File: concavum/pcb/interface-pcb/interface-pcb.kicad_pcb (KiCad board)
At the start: 2 copper layers, 29 x 40 mm, 19 parts, among them J1 PJ-342CB-TX-SMT, P1 ISP Pads, U1 ATMEGA32U4-MUR, U3 MCP23017-E/SO, X1 16MHz

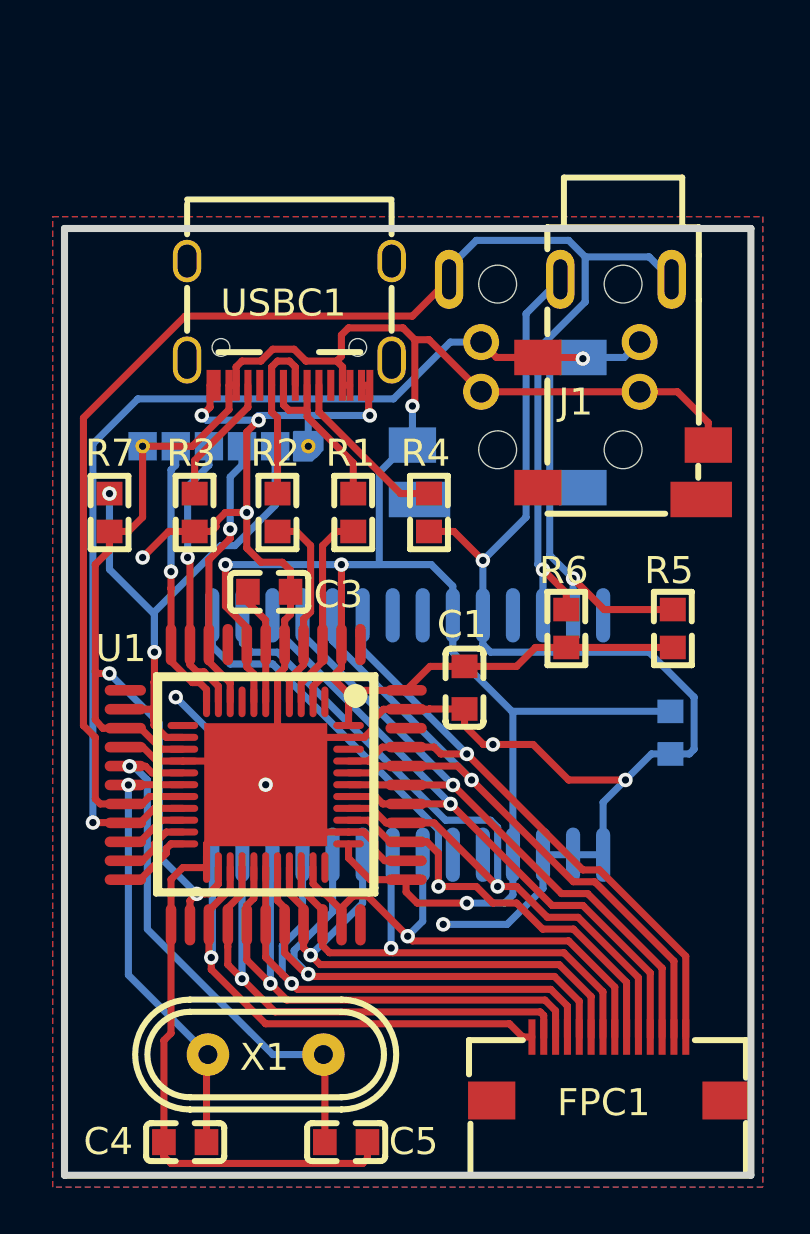
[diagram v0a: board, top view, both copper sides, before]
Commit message: Redo interface PCB using KiCad
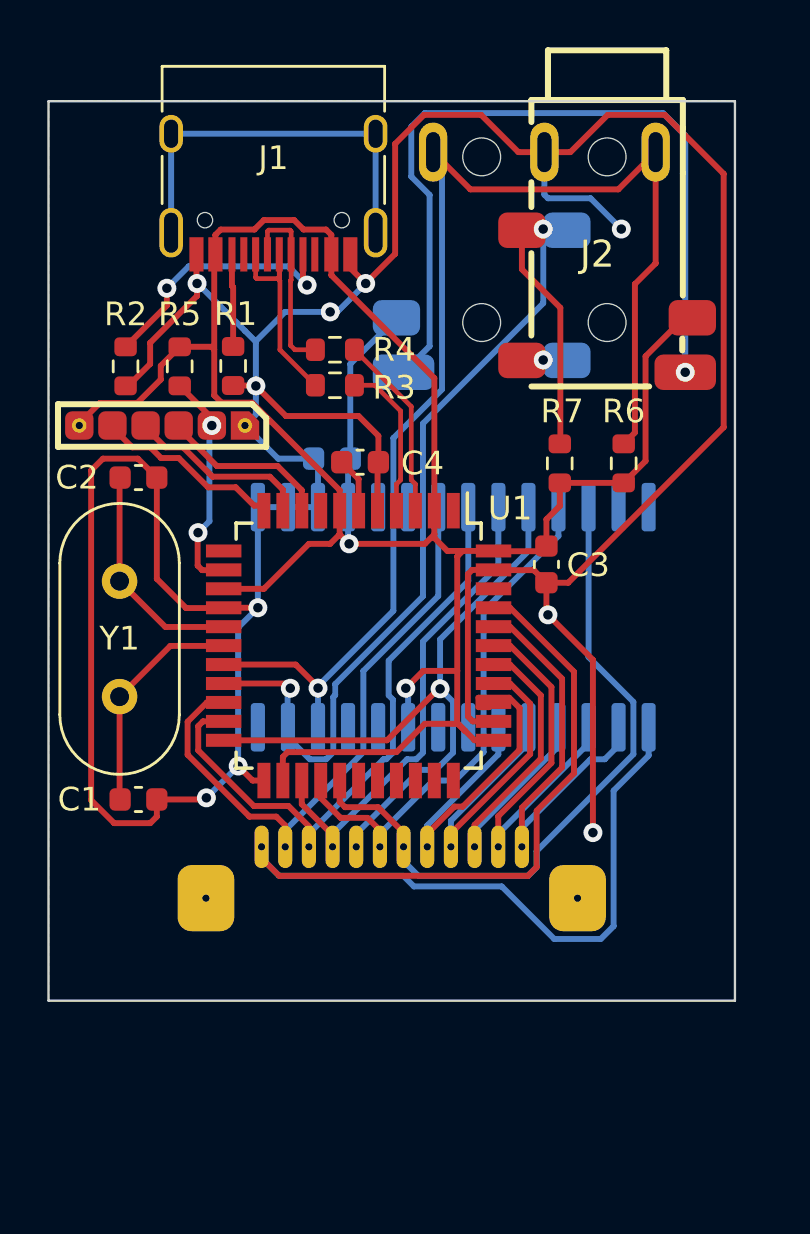
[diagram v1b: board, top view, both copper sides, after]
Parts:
- removed FPC1: AFC01-S14FCC-00, easyeda:FPC-SMD_14P-P0.50_AFC01-S14FCC-00
- removed P1: ISP Pads, easyeda:ISP PADS
- removed U3: MCP23017-E/SO, easyeda:SOIC-28_L18.1-W10.3-P1.27-LS10.3-BL
- removed USBC1: TYPE-C-31-M-12, easyeda:USB-C_SMD-TYPE-C-31-M-12
- removed X1: 16MHz, easyeda:HC-49US_L11.0-W4.6-P4.88
- added J2: Audio_Jack, Custom:Audio-Jack-Dual-Side, F.Cu at (163.6, 86.8)
- added J3: ISP_pads, Custom:ISP-Pads, F.Cu at (148.3, 93.7)
- added J4: FPC_connector, Custom:FPC-Connector, F.Cu at (154.5, 111.5)
- added U2: MCP23017_SO, Package_SO:SOIC-28W_7.5x17.9mm_P1.27mm, B.Cu at (157.1, 101.8)
- added Y1: Crystal_16MHz, Crystal:Crystal_HC49-4H_Vertical, F.Cu at (143.0, 105.2)
- C1, C2: value 100n -> 22p; footprint easyeda:C0603 -> Capacitor_SMD:C_0603_1608Metric
- C3: value 1u -> 100n; footprint easyeda:C0603 -> Capacitor_SMD:C_0603_1608Metric
- C4: value 22p -> 1u; footprint easyeda:C0603 -> Capacitor_SMD:C_0603_1608Metric
- C5: value 22p -> 100n; footprint easyeda:C0603 -> Capacitor_SMD:C_0603_1608Metric; moved to B.Cu
- J1: value PJ-342CB-TX-SMT -> USB_C_Port; footprint easyeda:AUDIO-SMD_PJ-342CB-TX-SMT DUAL SIDE HOLES -> Connector_USB:USB_C_Receptacle_HRO_TYPE-C-31-M-12
- R1, R2: value 22 -> 5.1k; footprint easyeda:R0603 -> Resistor_SMD:R_0603_1608Metric
- R3, R4: value 5.1k -> 22; footprint easyeda:R0603 -> Resistor_SMD:R_0603_1608Metric
- R5: value 1k -> 5.1k; footprint easyeda:R0603 -> Resistor_SMD:R_0603_1608Metric
- R6: footprint easyeda:R0603 -> Resistor_SMD:R_0603_1608Metric
- R7: value 5.1k -> 1k; footprint easyeda:R0603 -> Resistor_SMD:R_0603_1608Metric
- U1: value ATMEGA32U4-MUR -> ATmega32U4-A; footprint easyeda:QFN-44 QFP-44 -> Package_QFP:TQFP-44_10x10mm_P0.8mm
- moved C4 29.7 mm to (153.2, 95.2)
- moved C5 28.9 mm to (152.0, 95.1)
- moved C2 24.9 mm to (143.8, 95.9), turned to 0 degrees
- moved R5 23.6 mm to (145.5, 91.2), turned to 90 degrees
- moved R7 19.1 mm to (161.6, 95.3)
- moved J1 17.7 mm to (149.5, 82.4), turned to 180 degrees
- moved C1 14.6 mm to (143.8, 109.5), turned to 0 degrees
- moved C3 11.8 mm to (161.0, 99.6), turned to -90 degrees
- moved R2 8.91 mm to (143.3, 91.2), turned to -90 degrees
- moved R1 8.00 mm to (147.8, 91.2), turned to -90 degrees
- moved R3 8.00 mm to (152.1, 92.0), turned to 0 degrees
- moved R4 7.94 mm to (152.1, 90.5), turned to 0 degrees
- moved R6 7.39 mm to (164.3, 95.3)
- moved U1 7.07 mm to (153.1, 103.0), turned to -90 degrees
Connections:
- C1 pad 1: GND -> /XTAL1
- C1 pad 2: +5V -> GND
- C2 pad 1: GND -> /XTAL2
- C2 pad 2: +5V -> GND
- C3 pad 1: GND -> +5V
- C3 pad 2: U1_6 -> GND
- C4 pad 1: GND -> Net-(C4-Pad1)
- C4 pad 2: XTAL1 -> GND
- C5 pad 1: GND -> +5V
- C5 pad 2: XTAL2 -> GND
- R1 pad 1: RD- -> Net-(J1-PadB5)
- R1 pad 2: D- -> GND
- R2 pad 1: RD+ -> Net-(J1-PadA5)
- R2 pad 2: D+ -> GND
- R3 pad 1: GND -> /D+
- R3 pad 2: USBC1_B5 -> /DR+
- R4 pad 1: GND -> /D-
- R4 pad 2: USBC1_A5 -> /DR-
- R5 pad 1: SDA -> /RST
- R6 pad 1: SCL -> /SCL
- R7 pad 1: RST -> /SDA
- U1 pad 1: (no net) -> unconnected-(U1-Pad1)
- U1 pad 10: MOSI -> /MOSI
- U1 pad 11: MISO -> /MISO
- U1 pad 12: (no net) -> unconnected-(U1-Pad12)
- U1 pad 13: RST -> /RST
- U1 pad 16: XTAL2 -> /XTAL2
- U1 pad 17: XTAL1 -> /XTAL1
- U1 pad 18: SCL -> /SCL
- U1 pad 19: SDA -> /SDA
- U1 pad 20: (no net) -> /COL1
- U1 pad 21: (no net) -> /COL2
- U1 pad 22: (no net) -> /COL4
- U1 pad 25: COL1 -> /COL3
- U1 pad 26: COL2 -> /COL5
- U1 pad 27: COL3 -> /COL6
- U1 pad 28: COL4 -> unconnected-(U1-Pad28)
- U1 pad 29: COL5 -> unconnected-(U1-Pad29)
- U1 pad 3: RD- -> /DR-
- U1 pad 30: COL6 -> unconnected-(U1-Pad30)
- U1 pad 31: COL7 -> unconnected-(U1-Pad31)
- U1 pad 32: COL8 -> unconnected-(U1-Pad32)
- U1 pad 33: (no net) -> unconnected-(U1-Pad33)
- U1 pad 36: ROW1 -> /ROW2
- U1 pad 37: ROW2 -> /ROW3
- U1 pad 38: ROW3 -> /ROW4
- U1 pad 39: ROW4 -> /ROW5
- U1 pad 4: RD+ -> /DR+
- U1 pad 40: ROW5 -> /ROW6
- U1 pad 41: ROW6 -> /ROW1
- U1 pad 42: (no net) -> unconnected-(U1-Pad42)
- U1 pad 6: U1_6 -> Net-(C4-Pad1)
- U1 pad 8: (no net) -> unconnected-(U1-Pad8)
- U1 pad 9: SCK -> /SCK
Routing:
- net SCL: track 67.3 -> 0.00 mm, vias 1 -> 0
- net SDA: track 62.8 -> 0.00 mm, vias 3 -> 0
- net /SCL: track 0.00 -> 54.6 mm, vias 0 -> 1
- net /ROW1: track 0.00 -> 52.0 mm
- net /SDA: track 0.00 -> 42.9 mm, vias 0 -> 2
- net +5V: track 145.6 -> 104.9 mm, vias 6 -> 2
- net ROW2: track 35.4 -> 0.00 mm, vias 1 -> 0
- net ROW1: track 34.2 -> 0.00 mm, vias 1 -> 0
- net unconnected-(J2-PadTN): track 0.00 -> 33.4 mm, vias 0 -> 1
- net ROW5: track 29.9 -> 0.00 mm, vias 1 -> 0
- net ROW3: track 29.6 -> 0.00 mm, vias 1 -> 0
- net ROW6: track 29.2 -> 0.00 mm, vias 1 -> 0
- net ROW4: track 29.2 -> 0.00 mm, vias 1 -> 0
- net /COL6: track 0.00 -> 28.8 mm
- net /COL4: track 0.00 -> 28.2 mm, vias 0 -> 1
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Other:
- board size 29 x 40 mm -> 29 x 38 mm

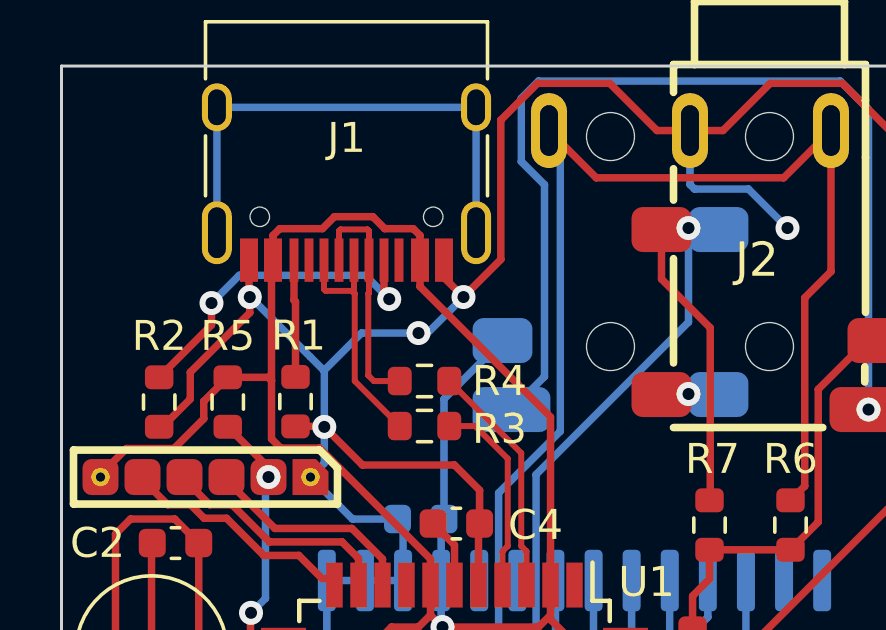
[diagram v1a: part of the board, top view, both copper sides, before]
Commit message: Add a 10µF capacitor as desrcibed in the datasheet
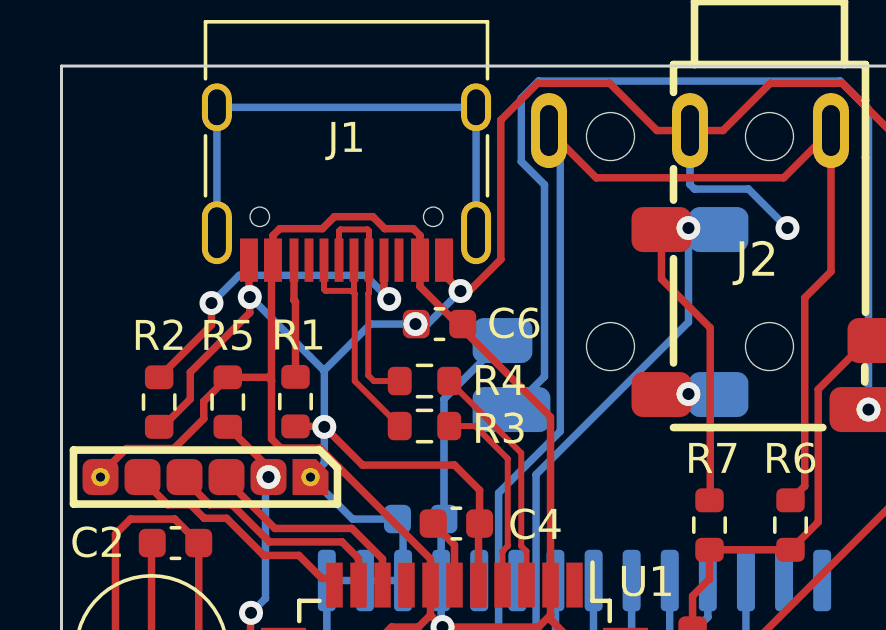
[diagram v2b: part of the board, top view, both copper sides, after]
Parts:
- added C6: 10u, Capacitor_SMD:C_0603_1608Metric, F.Cu at (152.6, 88.6)
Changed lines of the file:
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@@
   (net 52 "unconnected-(J1-PadB8)")
   (net 53 "unconnected-(J1-PadA8)")
+  (footprint "Capacitor_SMD:C_0603_1608Metric" (layer "F.Cu")
+    (at 152.6 88.6 180)
+    (descr "Capacitor SMD 0603 (1608 Metric), square (rectangular) end terminal, IPC_7351 nominal, (Body size source: IPC-SM-782 page 76, https://www.pcb-3d.com/wordpress/wp-content/uploads/ipc-sm-782a_amendment_1_and_2.pdf), generated with kicad-footprint-generator")
+    (tags "capacitor")
+    (property "Sheetfile" "interface-pcb.kicad_sch")
+    (property "Sheetname" "")
+    (attr smd)
+    (fp_text reference "C6" (at -2.5 0) (layer "F.SilkS")
+      (effects (font (size 1 1) (thickness 0.15)))
+    )
+    (fp_text value "10u" (at 2.8 0) (layer "F.Fab")
+      (effects (font (size 1 1) (thickness 0.15)))
+    )
+    (fp_text user "${REFERENCE}" (at 0 0) (layer "F.Fab")
+      (effects (font (size 0.4 0.4) (thickness 0.06)))
+    )
+    (fp_line (start -0.14058 -0.51) (end 0.14058 -0.51) (layer "F.SilkS") (width 0.12))
+    (fp_line (start -0.14058 0.51) (end 0.14058 0.51) (layer "F.SilkS") (width 0.12))
+    (fp_line (start 1.48 -0.73) (end 1.48 0.73) (layer "F.CrtYd") (width 0.05))
+    (fp_line (start -1.48 -0.73) (end 1.48 -0.73) (layer "F.CrtYd") (width 0.05))
+    (fp_line (start -1.48 0.73) (end -1.48 -0.73) (layer "F.CrtYd") (width 0.05))
+    (fp_line (start 1.48 0.73) (end -1.48 0.73) (layer "F.CrtYd") (width 0.05))
+    (fp_line (start -0.8 0.4) (end -0.8 -0.4) (layer "F.Fab") (width 0.1))
+    (fp_line (start 0.8 0.4) (end -0.8 0.4) (layer "F.Fab") (width 0.1))
+    (fp_line (start -0.8 -0.4) (end 0.8 -0.4) (layer "F.Fab") (width 0.1))
+    (fp_line (start 0.8 -0.4) (end 0.8 0.4) (layer "F.Fab") (width 0.1))
+    (pad "1" smd roundrect locked (at -0.775 0 180) (size 0.9 0.95) (layers "F.Cu" "F.Paste" "F.Mask") (roundrect_rratio 0.25)
+      (net 4 "+5V") (pintype "passive"))
+    (pad "2" smd roundrect locked (at 0.775 0 180) (size 0.9 0.95) (layers "F.Cu" "F.Paste" "F.Mask") (roundrect_rratio 0.25)
+      (net 2 "GND") (pintype "passive"))
+    (model "${KICAD6_3DMODEL_DIR}/Capacitor_SMD.3dshapes/C_0603_1608Metric.wrl"
+      (offset (xyz 0 0 0))
+      (scale (xyz 1 1 1))
+      (rotate (xyz 0 0 0))
+    )
+  )
   (footprint "Resistor_SMD:R_0603_1608Metric" (layer "F.Cu")
     (at 143.256 91.2 -90)
@@
   (segment (start 161.036 101.636) (end 161.1 101.7) (width 0.25) (layer "F.Cu") (net 2))
   (segment (start 160.505 99.812) (end 161.036 100.343) (width 0.25) (layer "F.Cu") (net 2))
-  (segment (start 153.4 87.7) (end 153.4 87.691047) (width 0.25) (layer "F.Cu") (net 2))
   (segment (start 144.575 110.225) (end 144.575 109.5) (width 0.25) (layer "F.Cu") (net 2))
   (segment (start 163 103.6) (end 163 110.9) (width 0.25) (layer "F.Cu") (net 2))
   (segment (start 146.25 87.67402) (end 146.27598 87.7) (width 0.25) (layer "F.Cu") (net 2))
   (segment (start 144.29296 91.1) (end 143.36796 92.025) (width 0.25) (layer "F.Cu") (net 2))
-  (segment (start 159.85 82.15) (end 160.95 82.15) (width 0.25) (layer "F.Cu") (net 2))
+  (segment (start 152.75 86.95) (end 152.75 86.47) (width 0.25) (layer "F.Cu") (net 2))
   (segment (start 153.9 95.541) (end 154.191 95.25) (width 0.25) (layer "F.Cu") (net 2))
   (segment (start 146.27598 87.7) (end 146.27598 88.22402) (width 0.25) (layer "F.Cu") (net 2))
   (segment (start 144.575 95.9) (end 143.775 95.1) (width 0.25) (layer "F.Cu") (net 2))
-  (segment (start 154.64452 81.798012) (end 155.867052 80.57548) (width 0.25) (layer "F.Cu") (net 2))
-  (segment (start 153.4 87.7) (end 152.75 87.05) (width 0.25) (layer "F.Cu") (net 2))
-  (segment (start 153.4 87.691047) (end 154.64452 86.446527) (width 0.25) (layer "F.Cu") (net 2))
+  (segment (start 159.85 82.15) (end 160.95 82.15) (width 0.25) (layer "F.Cu") (net 2))
   (segment (start 157.925978 106.2) (end 157.718051 105.992073) (width 0.25) (layer "F.Cu") (net 2))
   (segment (start 146.27598 88.22402) (end 144.29296 90.20704) (width 0.25) (layer "F.Cu") (net 2))
@@
   (segment (start 153.937 95.25) (end 153.937 94.137) (width 0.25) (layer "F.Cu") (net 2))
   (segment (start 148.624598 108.7) (end 148.012299 108.087701) (width 0.25) (layer "F.Cu") (net 2))
-  (segment (start 158.27548 80.57548) (end 159.85 82.15) (width 0.25) (layer "F.Cu") (net 2))
+  (segment (start 153.3 87.5) (end 152.75 86.95) (width 0.25) (layer "F.Cu") (net 2))
+  (segment (start 153.3 87.5) (end 153.591047 87.5) (width 0.25) (layer "F.Cu") (net 2))
+  (segment (start 154.64452 81.798012) (end 155.867052 80.57548) (width 0.25) (layer "F.Cu") (net 2))
+  (segment (start 155.867052 80.57548) (end 158.27548 80.57548) (width 0.25) (layer "F.Cu") (net 2))
   (segment (start 142.3 95.1) (end 141.8 95.6) (width 0.25) (layer "F.Cu") (net 2))
+  (segment (start 153.591047 87.5) (end 154.64452 86.446527) (width 0.25) (layer "F.Cu") (net 2))
   (segment (start 144.575 100.175) (end 144.575 95.9) (width 0.25) (layer "F.Cu") (net 2))
   (segment (start 145.812 101.412) (end 144.575 100.175) (width 0.25) (layer "F.Cu") (net 2))
@@
   (segment (start 148.760218 92.028168) (end 148.74305 92.011) (width 0.25) (layer "F.Cu") (net 2))
   (segment (start 157.718051 105.992073) (end 157.718051 99.981949) (width 0.25) (layer "F.Cu") (net 2))
-  (segment (start 155.867052 80.57548) (end 158.27548 80.57548) (width 0.25) (layer "F.Cu") (net 2))
+  (segment (start 158.27548 80.57548) (end 159.85 82.15) (width 0.25) (layer "F.Cu") (net 2))
+  (segment (start 154.64452 86.446527) (end 154.64452 81.798012) (width 0.25) (layer "F.Cu") (net 2))
   (segment (start 161.1 101.7) (end 163 103.6) (width 0.25) (layer "F.Cu") (net 2))
   (segment (start 153.9 97.082) (end 153.9 95.541) (width 0.25) (layer "F.Cu") (net 2))
   (segment (start 143.36796 92.025) (end 143.256 92.025) (width 0.25) (layer "F.Cu") (net 2))
-  (segment (start 152.75 87.05) (end 152.75 86.47) (width 0.25) (layer "F.Cu") (net 2))
-  (segment (start 154.64452 86.446527) (end 154.64452 81.798012) (width 0.25) (layer "F.Cu") (net 2))
   (segment (start 157.718051 99.981949) (end 157.9 99.8) (width 0.25) (layer "F.Cu") (net 2))
   (segment (start 147.169 101.412) (end 145.812 101.412) (width 0.25) (layer "F.Cu") (net 2))
@@
   (segment (start 161.036 100.343) (end 161.957 100.343) (width 0.25) (layer "F.Cu") (net 2))
   (segment (start 166.032948 80.57548) (end 163.62452 80.57548) (width 0.25) (layer "F.Cu") (net 2))
-  (via (at 151.9 88.9) (size 0.8) (drill 0.4) (layers "F.Cu" "B.Cu") (net 2))
+  (via (at 151.8 88.6) (size 0.8) (drill 0.4) (layers "F.Cu" "B.Cu") (net 2))
   (via (at 161.1 101.7) (size 0.8) (drill 0.4) (layers "F.Cu" "B.Cu") (net 2))
   (via (at 146.27598 87.7) (size 0.8) (drill 0.4) (layers "F.Cu" "B.Cu") (net 2))
@@
   (via (at 163 110.9) (size 0.8) (drill 0.4) (layers "F.Cu" "B.Cu") (net 2))
   (via (at 148.760218 92.028168) (size 0.8) (drill 0.4) (layers "F.Cu" "B.Cu") (net 2))
-  (via (at 153.4 87.7) (size 0.8) (drill 0.4) (layers "F.Cu" "B.Cu") (net 2))
+  (via (at 153.3 87.5) (size 0.8) (drill 0.4) (layers "F.Cu" "B.Cu") (net 2))
   (segment (start 148.845 101.4) (end 148.012299 102.232701) (width 0.25) (layer "B.Cu") (net 2))
+  (segment (start 152.2 88.6) (end 151.8 88.6) (width 0.25) (layer "B.Cu") (net 2))
   (segment (start 151.385 97.15) (end 151.385 95.285) (width 0.25) (layer "B.Cu") (net 2))
   (segment (start 146.669841 109.430159) (end 148.012299 108.087701) (width 0.25) (layer "B.Cu") (net 2))
-  (segment (start 152.2 88.9) (end 151.9 88.9) (width 0.25) (layer "B.Cu") (net 2))
-  (segment (start 150 88.9) (end 148.75 90.15) (width 0.25) (layer "B.Cu") (net 2))
   (segment (start 151.385 95.285) (end 151.2 95.1) (width 0.25) (layer "B.Cu") (net 2))
-  (segment (start 151.9 88.9) (end 150 88.9) (width 0.25) (layer "B.Cu") (net 2))
   (segment (start 151.2 95.1) (end 149.7 95.1) (width 0.25) (layer "B.Cu") (net 2))
   (segment (start 150.115 97.15) (end 151.385 97.15) (width 0.25) (layer "B.Cu") (net 2))
   (segment (start 162.9 84.1) (end 164.2 85.4) (width 0.25) (layer "B.Cu") (net 2))
+  (segment (start 151.8 88.6) (end 150.3 88.6) (width 0.25) (layer "B.Cu") (net 2))
   (segment (start 148.3 93.7) (end 148.760218 93.239782) (width 0.25) (layer "B.Cu") (net 2))
   (segment (start 148.760218 93.239782) (end 148.760218 90.160218) (width 0.25) (layer "B.Cu") (net 2))
@@
   (segment (start 148.3 89.7) (end 146.3 87.7) (width 0.25) (layer "B.Cu") (net 2))
   (segment (start 148.845 101.4) (end 148.845 97.15) (width 0.25) (layer "B.Cu") (net 2))
+  (segment (start 153.3 87.5) (end 152.2 88.6) (width 0.25) (layer "B.Cu") (net 2))
   (segment (start 148.012299 102.232701) (end 148.012299 108.087701) (width 0.25) (layer "B.Cu") (net 2))
-  (segment (start 153.4 87.7) (end 152.2 88.9) (width 0.25) (layer "B.Cu") (net 2))
   (segment (start 148.845 97.15) (end 150.115 97.15) (width 0.25) (layer "B.Cu") (net 2))
   (segment (start 149.7 95.1) (end 148.3 93.7) (width 0.25) (layer "B.Cu") (net 2))
+  (segment (start 150.3 88.6) (end 148.75 90.15) (width 0.25) (layer "B.Cu") (net 2))
   (segment (start 161.1 84.1) (end 162.9 84.1) (width 0.25) (layer "B.Cu") (net 2))
   (segment (start 146.3 87.7) (end 146.27598 87.7) (width 0.25) (layer "B.Cu") (net 2))
